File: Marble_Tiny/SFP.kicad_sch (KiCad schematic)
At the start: 85 parts, among them J1 TYCO_1888247-1, J11 TYCO_1888247-1, J12 TYCO_1888247-1, J13 TYCO_1888247-1, J8 2180739-1, J9 2180739-1, U17 TCA9535RTWR, U19 TCA9535RTWR, U26 PCA9546ARGV

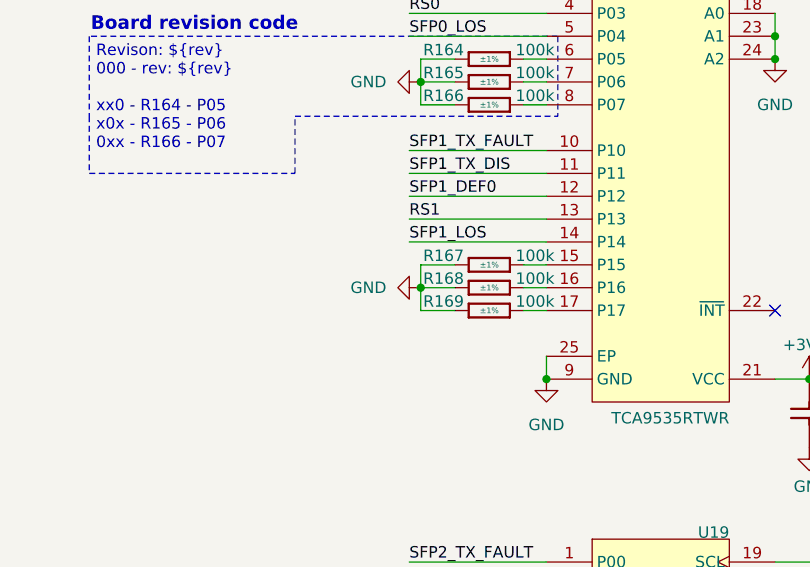
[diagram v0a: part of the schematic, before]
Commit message: connected more address lines to DDR, new board name
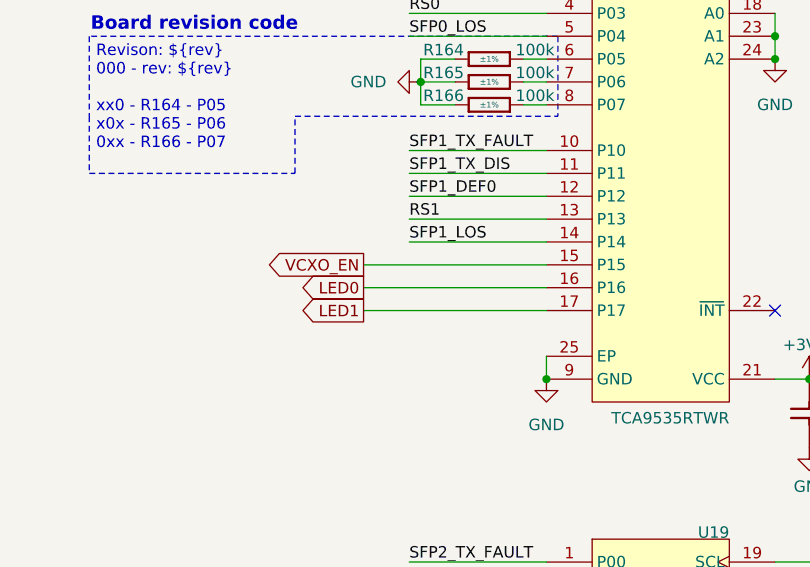
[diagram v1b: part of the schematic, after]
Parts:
- removed R167, R168, R169: R0402_100K_1%_0.0625W_100PPM, Resistors SMD:RESC1005X40N, symbol Resistors SMD:R0402_100K_1%_0.0625W_100PPM
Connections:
- net LED0: now reaches U17.16 (P16)
- net VCXO_EN: now reaches U17.15 (P15)
- net LED1: now reaches U17.17 (P17)
